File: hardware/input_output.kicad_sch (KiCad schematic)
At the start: 15 parts, among them J6 Conn_01x08, J7 Speaker, U7 PAM8302AAD

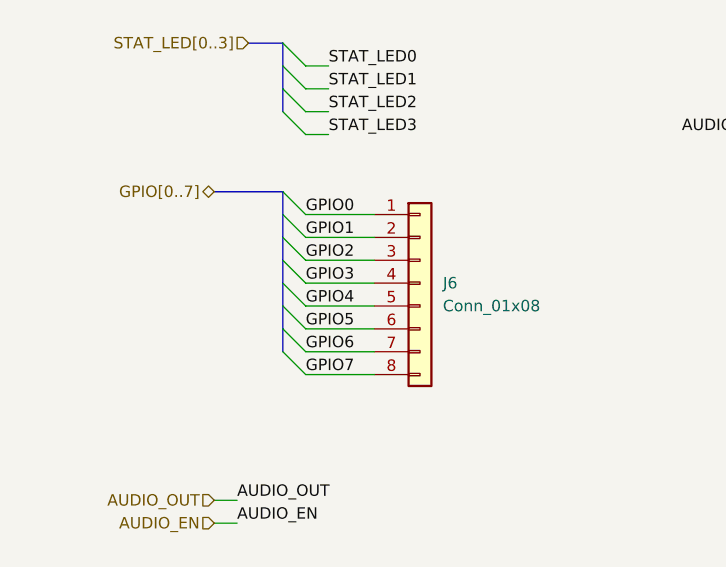
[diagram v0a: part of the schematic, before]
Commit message: [Hardware] Remove unused breakouts
* Remove extra GPIO and SPI outputs from MCU
* remove auxillary connectors for GPIO, SPI, and I2C
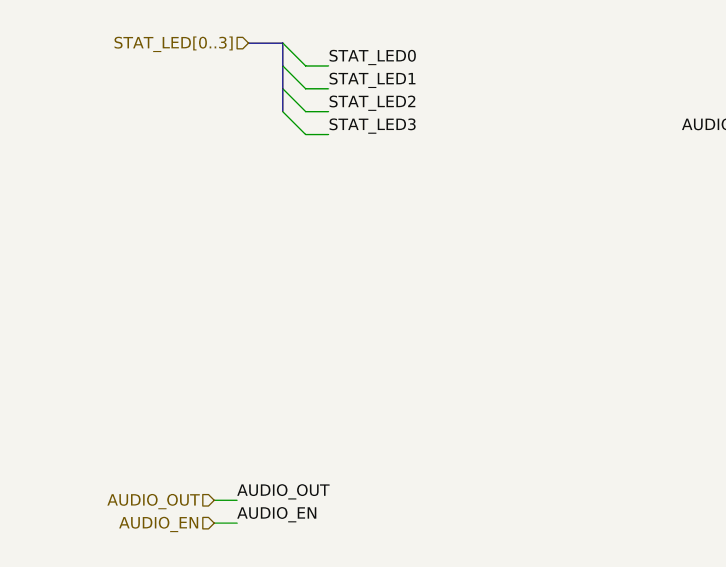
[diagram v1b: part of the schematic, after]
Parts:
- removed J6: Conn_01x08, Connector_PinHeader_1.27mm:PinHeader_1x08_P1.27mm_Vertical, symbol Connector_Generic:Conn_01x08

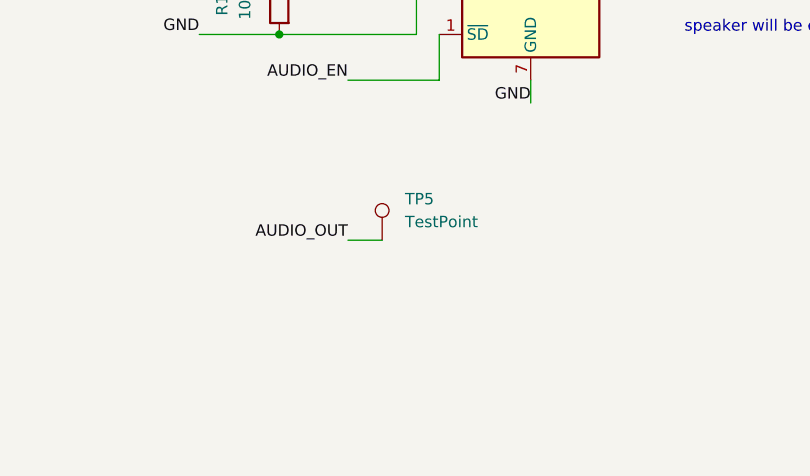
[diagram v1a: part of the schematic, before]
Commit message: [Hardware] Update testpoints
* Add TPs for I2C since we removed the I2C header
* Add ground testpoints for GPIO and audio out
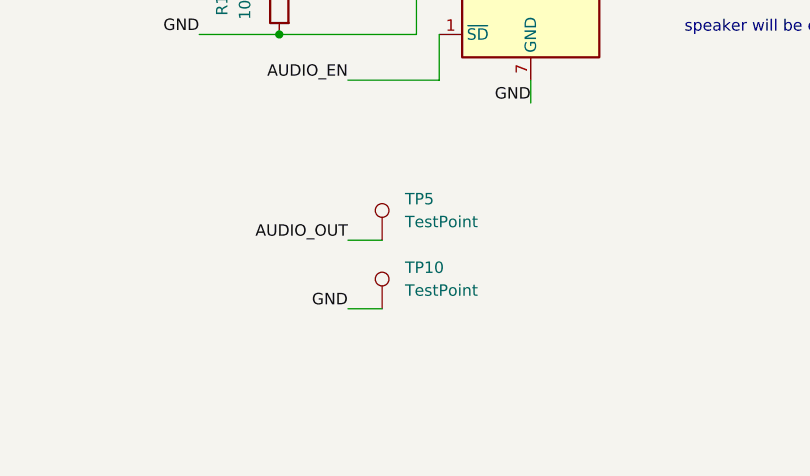
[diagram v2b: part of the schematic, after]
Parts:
- added TP10: TestPoint, Leaf_Jumper:TestPoint_0.5mm_1mm, symbol Connector:TestPoint
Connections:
- net GND: now also TP10.1
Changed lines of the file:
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@@
+	(wire
+		(pts
+			(xy 118.11 125.73) (xy 121.92 125.73)
+		)
+		(stroke
+			(width 0)
+			(type default)
+		)
+	)
 	(wire
 		(pts
@@
 	(label "LED_CTRL4"
 		(at 104.14 54.61 180)
+		(fields_autoplaced yes)
+		(effects
+			(font
+				(size 1.27 1.27)
+			)
+			(justify right bottom)
+		)
+	)
+	(label "GND"
+		(at 118.11 125.73 180)
 		(fields_autoplaced yes)
 		(effects
@@
 					(unit 1)
 				)
+			)
+		)
+	)
+	(symbol
+		(lib_id "Connector:TestPoint")
+		(at 121.92 125.73 0)
+		(unit 1)
+		(exclude_from_sim no)
+		(in_bom yes)
+		(on_board yes)
+		(dnp no)
+		(fields_autoplaced yes)
+		(property "Reference" "TP10"
+			(at 124.46 121.1579 0)
+			(effects
+				(font
+					(size 1.27 1.27)
+				)
+				(justify left)
+			)
+		)
+		(property "Value" "TestPoint"
+			(at 124.46 123.6979 0)
+			(effects
+				(font
+					(size 1.27 1.27)
+				)
+				(justify left)
+			)
+		)
+		(property "Footprint" "Leaf_Jumper:TestPoint_0.5mm_1mm"
+			(at 127 125.73 0)
+			(effects
+				(font
+					(size 1.27 1.27)
+				)
+				(hide yes)
+			)
+		)
+		(property "Datasheet" "~"
+			(at 127 125.73 0)
+			(effects
+				(font
+					(size 1.27 1.27)
+				)
+				(hide yes)
+			)
+		)
+		(property "Description" "test point"
+			(at 121.92 125.73 0)
+			(effects
+				(font
+					(size 1.27 1.27)
+				)
+				(hide yes)
+			)
+		)
+		(pin "1"
+		)
+		(instances
+			(project "holiday-widget"
+				(path "/addc3208-a9c4-4d28-9808-559c1d81e43b/0fdb39f4-f262-4df8-82d6-8f176468da30"
+					(reference "TP10")
+					(unit 1)
+				)

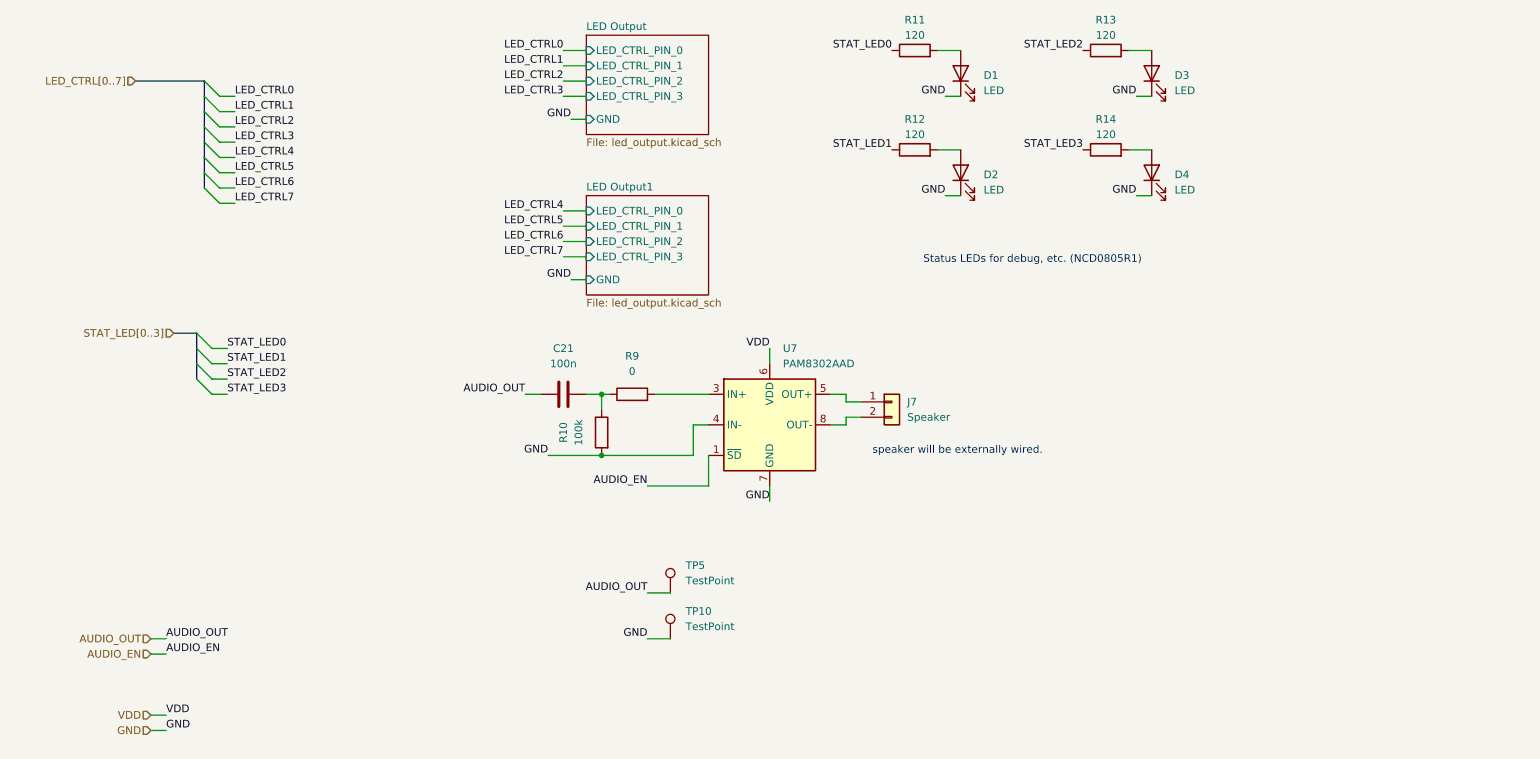
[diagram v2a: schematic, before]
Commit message: [Hardware] Update LEDs
Add additional LEDs and arrange in 7x7 matrix. Remove 2x status LEDs. Reroute MCU connetions to be more sensible. Rearrange components.
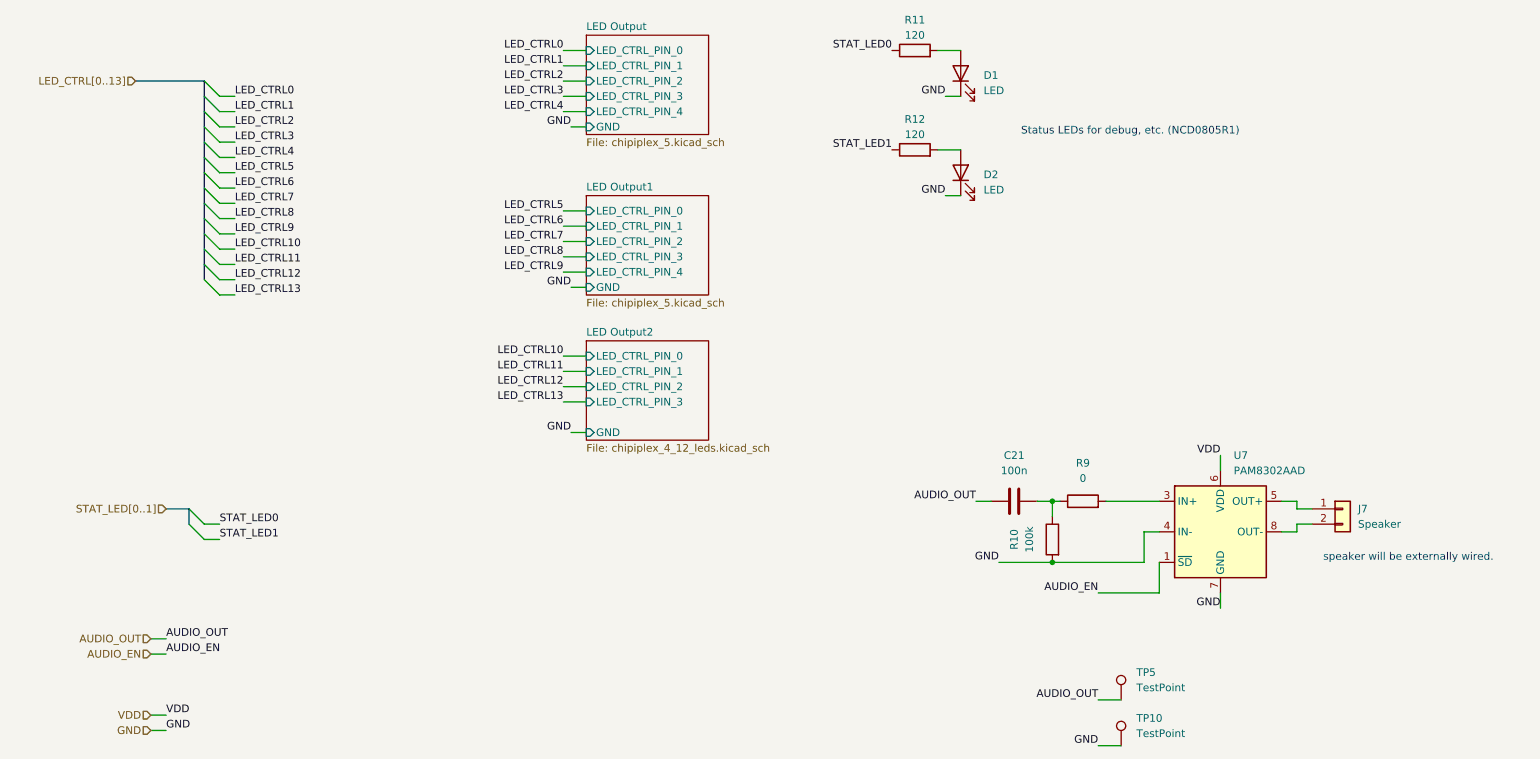
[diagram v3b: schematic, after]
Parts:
- removed D3, D4: LED, LED_SMD:LED_0805_2012Metric_Pad1.15x1.40mm_HandSolder, symbol Device:LED
- removed R13, R14: 120, Resistor_SMD:R_0603_1608Metric_Pad0.98x0.95mm_HandSolder, symbol Device:R
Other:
- added sheet LED Output2 (chipiplex_4_12_leds.kicad_sch)
- sheet LED Output: file led_output.kicad_sch -> chipiplex_5.kicad_sch
- sheet LED Output ports: added LED_CTRL_PIN_4; removed none
- sheet LED Output1: file led_output.kicad_sch -> chipiplex_5.kicad_sch
- sheet LED Output1 ports: added LED_CTRL_PIN_4; removed none
- moved on the sheet: C21, J7, R10, R9, TP10, TP5, U7

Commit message: Change many passives to 0402 and assign part numbers
Incorporate 0402 parts where possible
Assign Manufacturer Part Numbers to parts where possible
Update layout for the new passive sizes
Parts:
- C21: footprint Capacitor_SMD:C_0603_1608Metric_Pad1.08x0.95mm_HandSolder -> Capacitor_SMD:C_0402_1005Metric; MPN (none) -> CL05A104KA5NNNC
- D1, D2: MPN (none) -> LTST-C171GKT
- R10: footprint Resistor_SMD:R_0603_1608Metric_Pad0.98x0.95mm_HandSolder -> Resistor_SMD:R_0402_1005Metric; MPN (none) -> RC0402FR-07100KL
- R11, R12: footprint Resistor_SMD:R_0603_1608Metric_Pad0.98x0.95mm_HandSolder -> Resistor_SMD:R_0402_1005Metric; MPN (none) -> RC0402FR-07120RL
- R9: footprint Resistor_SMD:R_0603_1608Metric_Pad0.98x0.95mm_HandSolder -> Resistor_SMD:R_0402_1005Metric; MPN (none) -> RC0402JR-070RL
- U7: MPN (none) -> PAM8302AADCR
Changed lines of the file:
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@@
 			)
 		)
-		(property "Footprint" "Resistor_SMD:R_0603_1608Metric_Pad0.98x0.95mm_HandSolder"
+		(property "Footprint" "Resistor_SMD:R_0402_1005Metric"
 			(at 162.56 46.228 90)
 			(effects
@@
 		)
 		(property "Description" "Resistor"
+			(at 162.56 44.45 0)
+			(effects
+				(font
+					(size 1.27 1.27)
+				)
+				(hide yes)
+			)
+		)
+		(property "MPN" "RC0402FR-07120RL"
 			(at 162.56 44.45 0)
 			(effects
@@
 			)
 		)
+		(property "MPN" ""
+			(at 196.85 143.51 0)
+			(effects
+				(font
+					(size 1.27 1.27)
+				)
+				(hide yes)
+			)
+		)
 		(pin "1"
 		)
@@
 			)
 		)
+		(property "MPN" "LTST-C171GKT"
+			(at 170.18 48.26 0)
+			(effects
+				(font
+					(size 1.27 1.27)
+				)
+				(hide yes)
+			)
+		)
 		(pin "1"
 		)
@@
 			)
 		)
-		(property "Footprint" "Resistor_SMD:R_0603_1608Metric_Pad0.98x0.95mm_HandSolder"
+		(property "Footprint" "Resistor_SMD:R_0402_1005Metric"
 			(at 190.5 104.648 90)
 			(effects
@@
 			)
 		)
+		(property "MPN" "RC0402JR-070RL"
+			(at 190.5 102.87 0)
+			(effects
+				(font
+					(size 1.27 1.27)
+				)
+				(hide yes)
+			)
+		)
 		(pin "1"
 		)
@@
 			)
 		)
-		(property "Footprint" "Capacitor_SMD:C_0603_1608Metric_Pad1.08x0.95mm_HandSolder"
+		(property "Footprint" "Capacitor_SMD:C_0402_1005Metric"
 			(at 182.88 101.9048 0)
 			(effects
@@
 			)
 		)
+		(property "MPN" "CL05A104KA5NNNC"
+			(at 179.07 102.87 0)
+			(effects
+				(font
+					(size 1.27 1.27)
+				)
+				(hide yes)
+			)
+		)
 		(pin "1"
 		)
@@
 			)
 		)
-		(property "Footprint" "Resistor_SMD:R_0603_1608Metric_Pad0.98x0.95mm_HandSolder"
+		(property "Footprint" "Resistor_SMD:R_0402_1005Metric"
 			(at 162.56 29.718 90)
 			(effects
@@
 		)
 		(property "Description" "Resistor"
+			(at 162.56 27.94 0)
+			(effects
+				(font
+					(size 1.27 1.27)
+				)
+				(hide yes)
+			)
+		)
+		(property "MPN" "RC0402FR-07120RL"
 			(at 162.56 27.94 0)
 			(effects
@@
 			)
 		)
+		(property "MPN" ""
+			(at 196.85 135.89 0)
+			(effects
+				(font
+					(size 1.27 1.27)
+				)
+				(hide yes)
+			)
+		)
 		(pin "1"
 		)
@@
 			)
 		)
+		(property "MPN" "LTST-C171GKT"
+			(at 170.18 31.75 0)
+			(effects
+				(font
+					(size 1.27 1.27)
+				)
+				(hide yes)
+			)
+		)
 		(pin "1"
 		)
@@
 			)
 		)
+		(property "MPN" "PAM8302AADCR"
+			(at 213.36 107.95 0)
+			(effects
+				(font
+					(size 1.27 1.27)
+				)
+				(hide yes)
+			)
+		)
 		(pin "8"
 		)
@@
 			)
 		)
-		(property "Footprint" "Resistor_SMD:R_0603_1608Metric_Pad0.98x0.95mm_HandSolder"
+		(property "Footprint" "Resistor_SMD:R_0402_1005Metric"
 			(at 187.198 109.22 90)
 			(effects
@@
 		)
 		(property "Description" "Resistor"
+			(at 185.42 109.22 0)
+			(effects
+				(font
+					(size 1.27 1.27)
+				)
+				(hide yes)
+			)
+		)
+		(property "MPN" "RC0402FR-07100KL"
 			(at 185.42 109.22 0)
 			(effects
@@
 			(at 233.68 104.14 0)
 			(effects
+				(font
+					(size 1.27 1.27)
+				)
+				(hide yes)
+			)
+		)
+		(property "MPN" ""
+			(at 233.68 104.14 0)
+			(effects

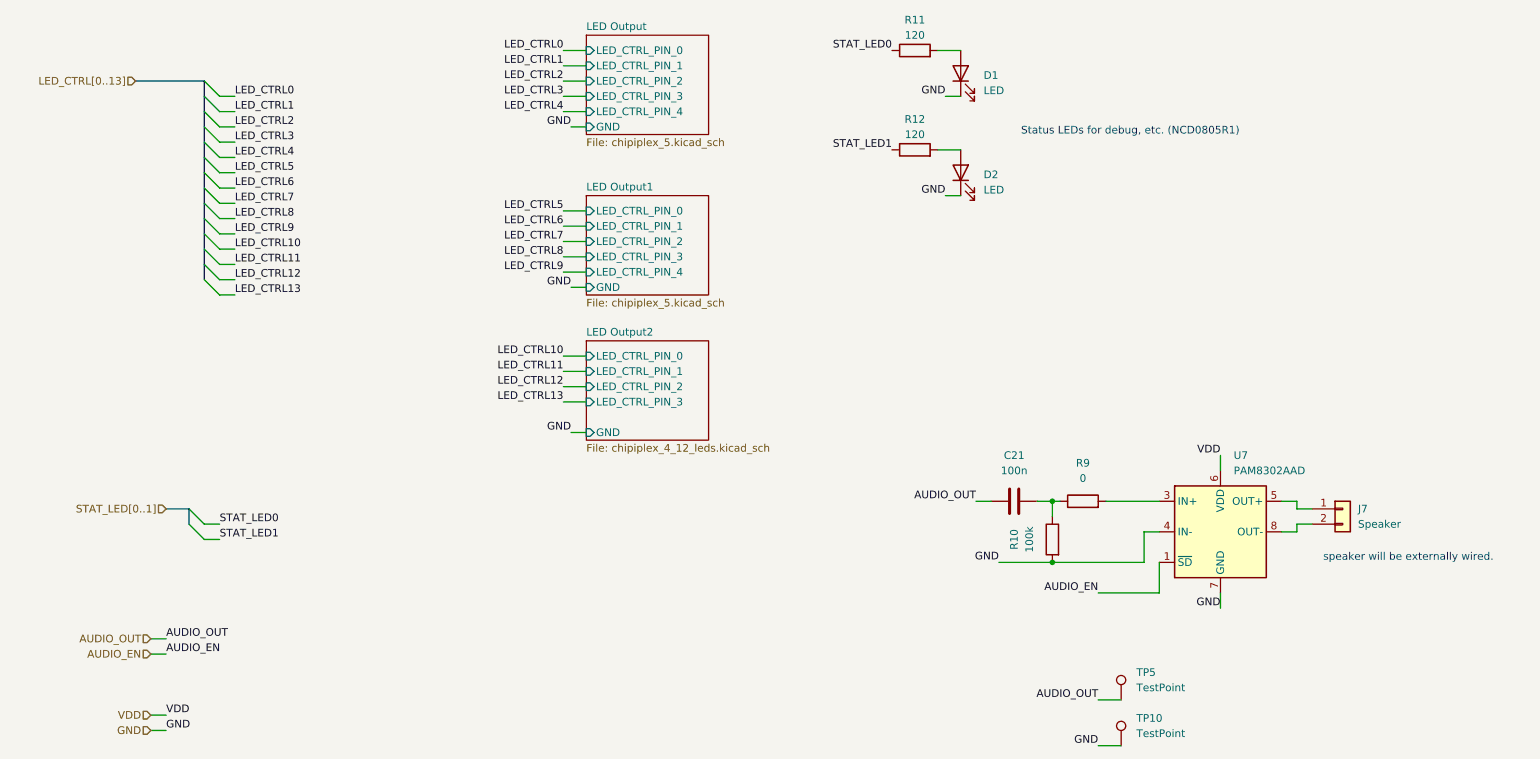
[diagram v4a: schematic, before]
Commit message: Remove status LEDs
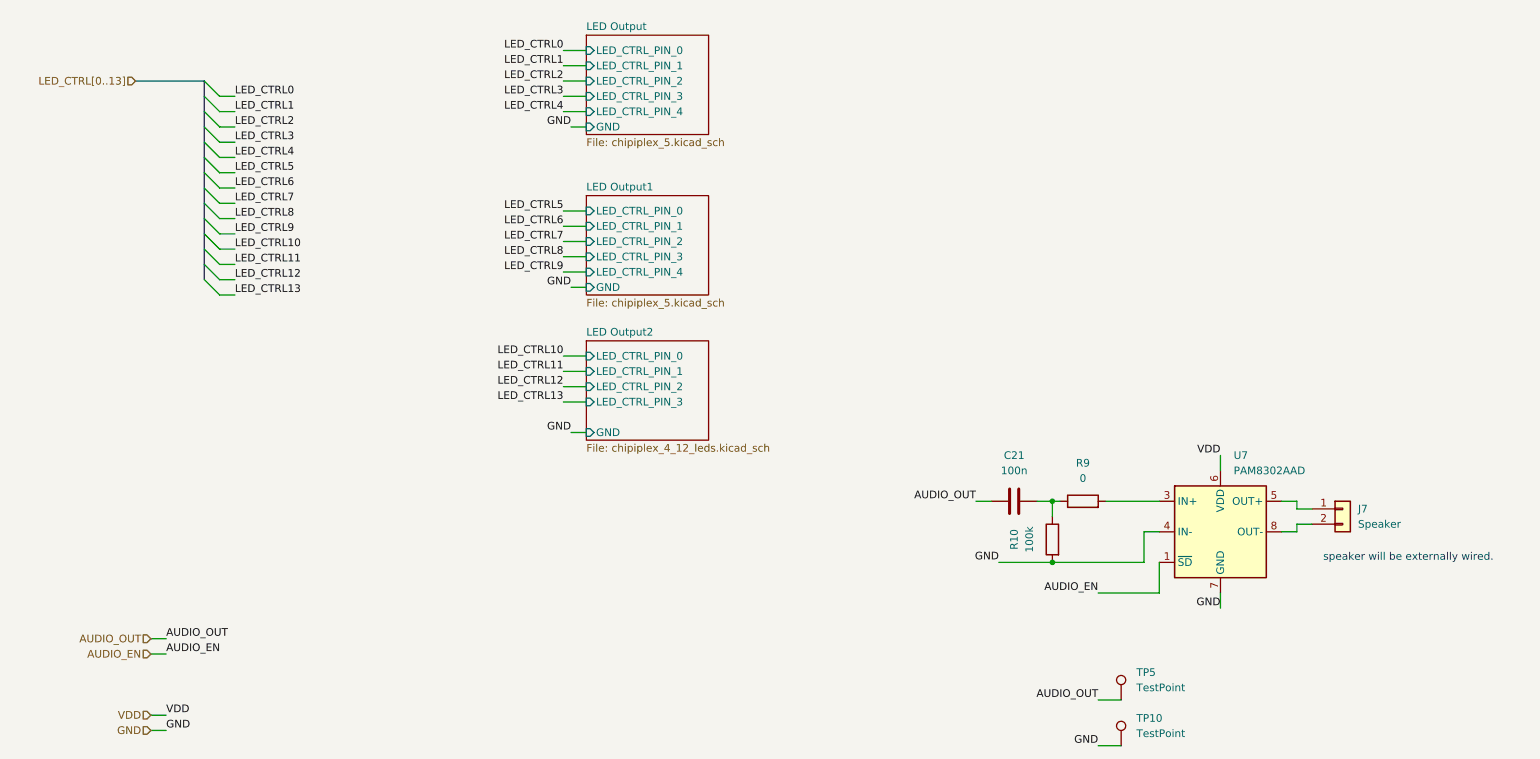
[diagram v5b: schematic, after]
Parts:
- removed D1, D2: LED, LED_SMD:LED_0805_2012Metric_Pad1.15x1.40mm_HandSolder, symbol Device:LED
- removed R11, R12: 120, Resistor_SMD:R_0402_1005Metric, symbol Device:R
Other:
- note removed: "Status LEDs for debug, etc. (NCD0805R1)"

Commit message: Add throughhole speaker
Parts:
- J7: footprint Connector_Wire:SolderWire-1sqmm_1x02_P5.4mm_D1.4mm_OD2.7mm -> holiday-widget:SPKR_AST-01508MR-WT-R
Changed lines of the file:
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@@
 			)
 		)
-		(property "Footprint" "Connector_Wire:SolderWire-1sqmm_1x02_P5.4mm_D1.4mm_OD2.7mm"
+		(property "Footprint" "holiday-widget:SPKR_AST-01508MR-WT-R"
 			(at 233.68 104.14 0)
 			(effects
